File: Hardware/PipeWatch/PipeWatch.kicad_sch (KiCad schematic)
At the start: 24 parts, among them J1 WJ126V-5.0-2P, U1 IRM-10-5_C20618064, U3 ESP32-S3-WROOM-1-N16R8, U5 XIAO-ESP32-S3-DIP

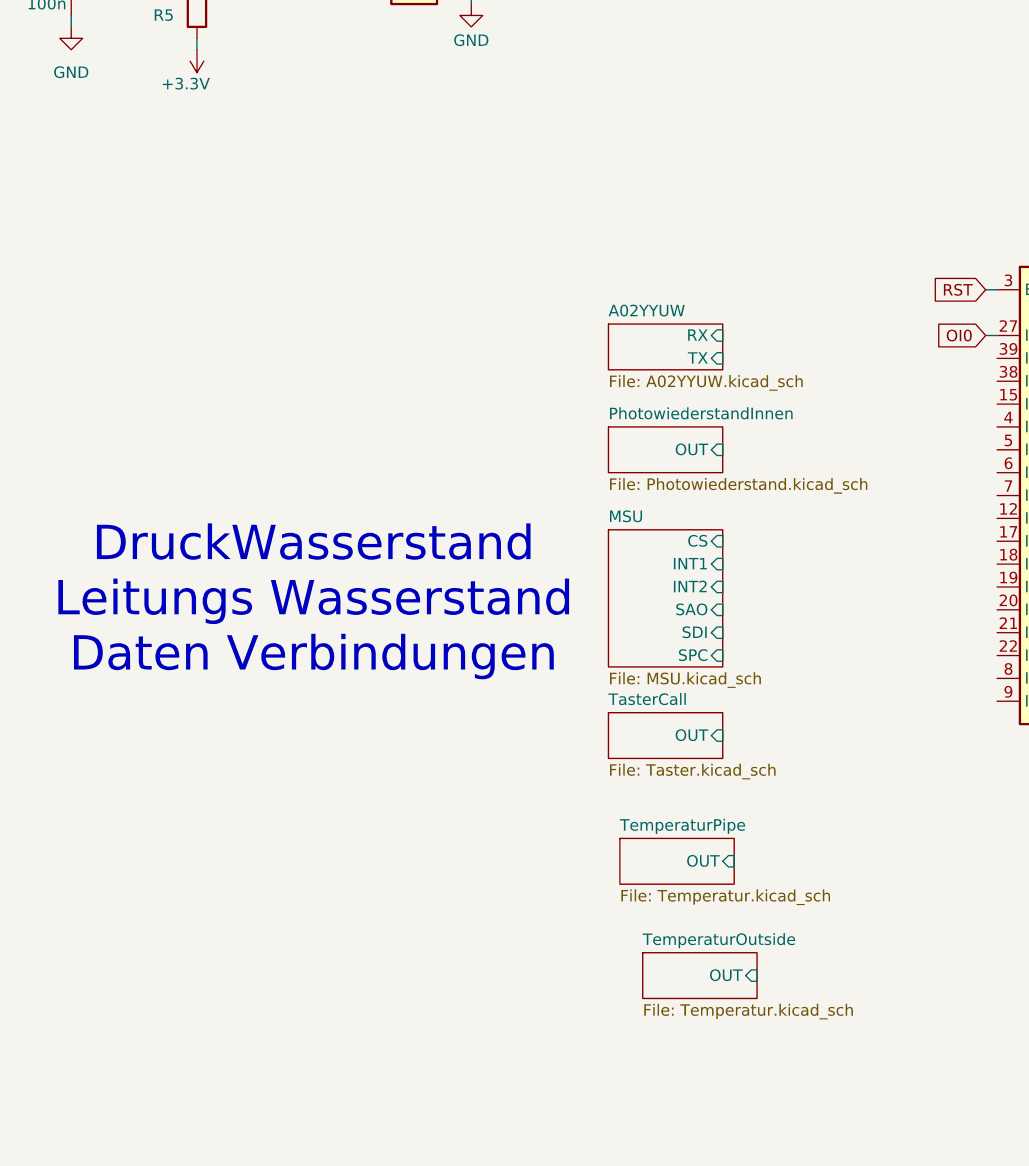
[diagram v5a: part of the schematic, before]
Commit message: added adc
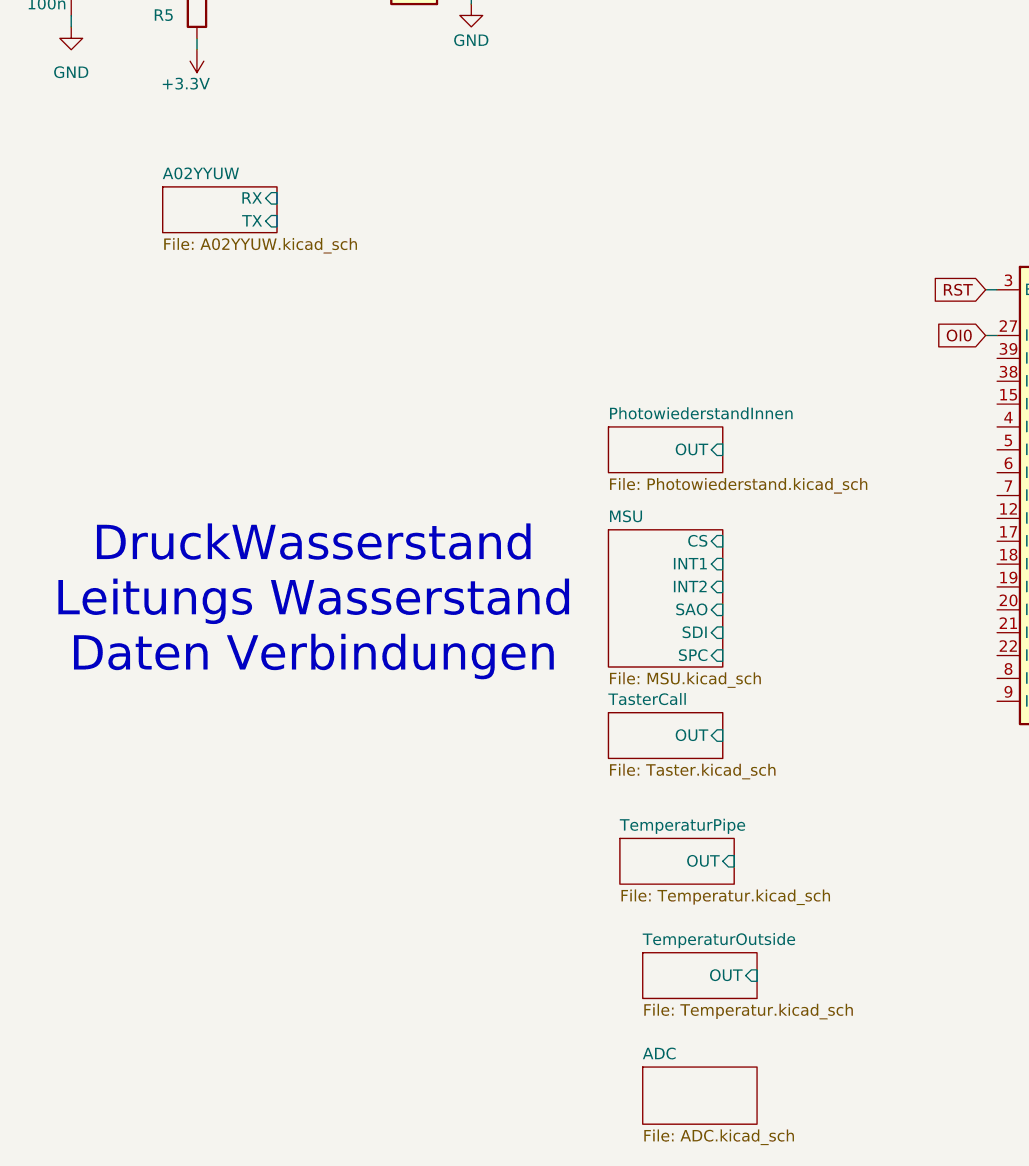
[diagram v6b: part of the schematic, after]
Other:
- added sheet ADC (ADC.kicad_sch)
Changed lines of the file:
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@@
+	)
+	(sheet
+		(at 90.17 176.53)
+		(size 12.7 6.35)
+		(exclude_from_sim no)
+		(in_bom yes)
+		(on_board yes)
+		(dnp no)
+		(fields_autoplaced yes)
+		(stroke
+			(width 0.1524)
+			(type solid)
+		)
+		(fill
+			(color 0 0 0 0.0000)
+		)
+		(property "Sheetname" "ADC"
+			(at 90.17 175.8184 0)
+			(effects
+				(font
+					(size 1.27 1.27)
+				)
+				(justify left bottom)
+			)
+		)
+		(property "Sheetfile" "ADC.kicad_sch"
+			(at 90.17 183.4646 0)
+			(effects
+				(font
+					(size 1.27 1.27)
+				)
+				(justify left top)
+			)
+		)
+		(instances
+			(project "PipeWatch"
+				(path "/149975cd-655c-40c3-be76-7a7ba16694c7"
+					(page "13")
+				)
+			)
+		)
 	)
 	(sheet
@@
 	)
 	(sheet
-		(at 86.36 93.98)
+		(at 36.83 78.74)
 		(size 12.7 5.08)
 		(exclude_from_sim no)
@@
 		)
 		(property "Sheetname" "A02YYUW"
-			(at 86.36 93.2684 0)
+			(at 36.83 78.0284 0)
 			(effects
 				(font
@@
 		)
 		(property "Sheetfile" "A02YYUW.kicad_sch"
-			(at 86.36 99.6446 0)
+			(at 36.83 84.4046 0)
 			(effects
 				(font
@@
 		)
 		(pin "RX" input
-			(at 99.06 95.25 0)
+			(at 49.53 80.01 0)
 			(effects
 				(font
@@
 		)
 		(pin "TX" input
-			(at 99.06 97.79 0)
-			(effects
-				(font
+			(at 49.53 82.55 0)
+			(effects
+				(font

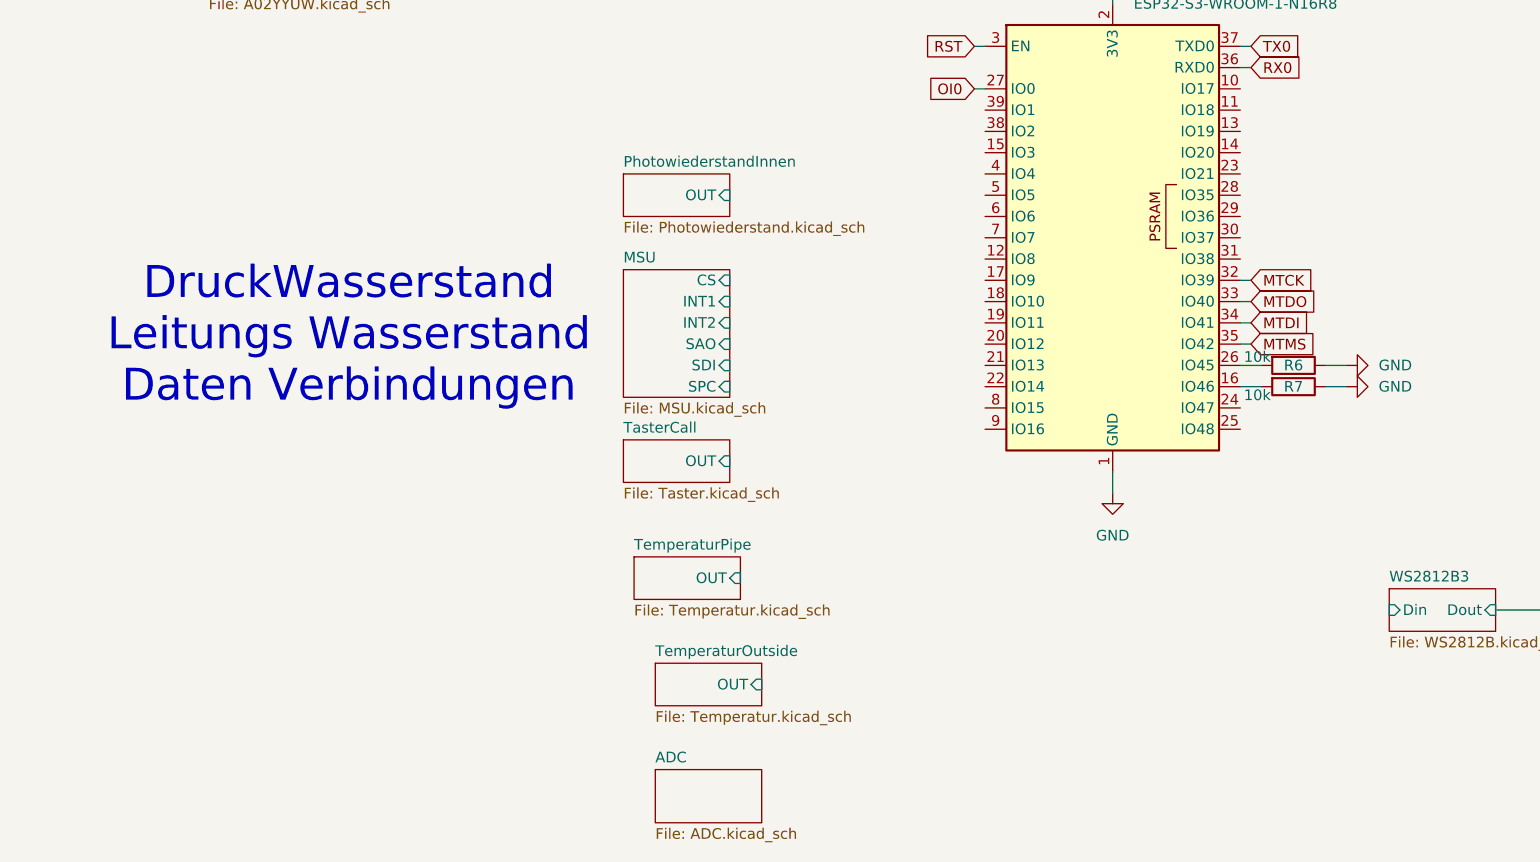
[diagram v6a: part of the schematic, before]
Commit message: Started laying traces
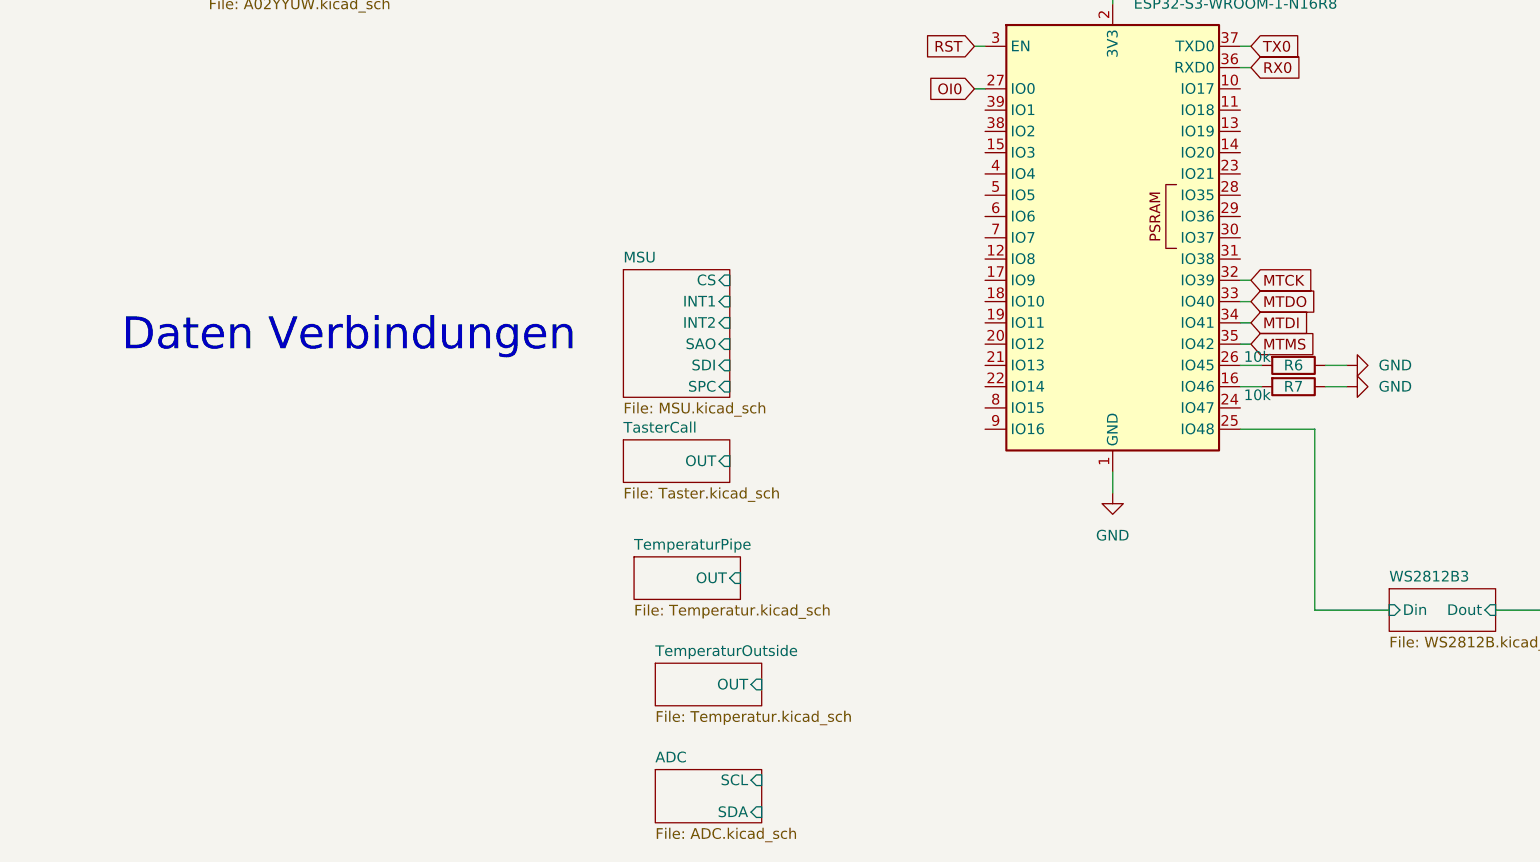
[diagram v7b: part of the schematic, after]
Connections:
- net WS2812B3/Din: now also U3.25 (IO48)
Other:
- removed sheet PhotowiederstandInnen
- sheet ADC ports: added SCL, SDA; removed none
- note added: "Daten Verbindungen"
- note removed: "DruckWasserstand Leitungs Wasserstand Daten Verbindungen"
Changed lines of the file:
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@@
 	(generator_version "9.0")
 	(paper "A4")
-	(text "DruckWasserstand\nLeitungs Wasserstand\nDaten Verbindungen"
+	(text "Daten Verbindungen"
 		(exclude_from_sim no)
 		(at 53.594 124.714 0)
@@
 	(wire
 		(pts
+			(xy 168.91 157.48) (xy 177.8 157.48)
+		)
+		(stroke
+			(width 0)
+			(type default)
+		)
+	)
+	(wire
+		(pts
 			(xy 106.68 29.21) (xy 106.68 30.48)
 		)
@@
 	(wire
 		(pts
+			(xy 160.02 135.89) (xy 168.91 135.89)
+		)
+		(stroke
+			(width 0)
+			(type default)
+		)
+	)
+	(wire
+		(pts
 			(xy 53.34 19.05) (xy 53.34 17.78)
 		)
@@
 	(wire
 		(pts
+			(xy 168.91 135.89) (xy 168.91 157.48)
+		)
+		(stroke
+			(width 0)
+			(type default)
+		)
+	)
+	(wire
+		(pts
 			(xy 153.67 63.5) (xy 157.48 63.5)
 		)
@@
 			)
 		)
+		(pin "SCL" input
+			(at 102.87 177.8 0)
+			(effects
+				(font
+					(size 1.27 1.27)
+				)
+				(justify right)
+			)
+		)
+		(pin "SDA" input
+			(at 102.87 181.61 0)
+			(effects
+				(font
+					(size 1.27 1.27)
+				)
+				(justify right)
+			)
+		)
 		(instances
 			(project "PipeWatch"
@@
 				)
 			)
-		)
-	)
-	(sheet
-		(at 86.36 105.41)
-		(size 12.7 5.08)
-		(exclude_from_sim no)
-		(in_bom yes)
-		(on_board yes)
-		(dnp no)
-		(fields_autoplaced yes)
-		(stroke
-			(width 0.1524)
-			(type solid)
-		)
-		(fill
-			(color 0 0 0 0.0000)
-		)
-		(property "Sheetname" "PhotowiederstandInnen"
-			(at 86.36 104.6984 0)
-			(effects
-				(font
-					(size 1.27 1.27)
-				)
-				(justify left bottom)
-			)
-		)
-		(property "Sheetfile" "Photowiederstand.kicad_sch"
-			(at 86.36 111.0746 0)
-			(effects
-				(font
-					(size 1.27 1.27)
-				)
-				(justify left top)
-			)
-		)
-		(property "Field2" ""
-			(at 86.36 105.41 0)
-			(effects
-				(font
-					(size 1.27 1.27)
-				)
-			)
-		)
-		(pin "OUT" input
-			(at 99.06 107.95 0)
-			(effects
-				(font
-					(size 1.27 1.27)
-				)
-				(justify right)
-			)
-		)
-		(instances
-			(project "PipeWatch"
-				(path "/149975cd-655c-40c3-be76-7a7ba16694c7"
-					(page "2")
-				)
-			)

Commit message: Final Version (Ordered it)
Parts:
- TP1: value Neopixel -> Neopxl
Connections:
- net WS2812B3/Din is gone; now on an unnamed net: U3.25 (IO48)
- net MSU/CS: now also U3.18 (IO10)
- net MSU/INT2: now also U3.17 (IO9)
- net MSU/SAO: now also U3.19 (IO11)
- net MSU/SDI: now also U3.20 (IO12)
- net MSU/SPC: now also U3.21 (IO13)
- net TasterCall/OUT: now also U3.14 (IO20)
- net TemperaturOutside/OUT: now also U3.31 (IO38)
- net TemperaturPipe/OUT: now also U3.38 (IO2)
- net Uart2_RX: now reaches U3.12 (IO8)
- net Uart2_TX: now reaches U3.13 (IO19)
- net MSU_INT1: now reaches U3.15 (IO3)
- net ADC_SDA: now reaches U3.22 (IO14)
- net ADC_SCL: now reaches U3.23 (IO21)
- net at U3.24 (IO47): now also U5.7 (U0TXD/D6/TX)
- net WS2812B Data: now reaches U3.39 (IO1)
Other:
- note removed: "Daten Verbindungen"
- moved on the sheet: U5
